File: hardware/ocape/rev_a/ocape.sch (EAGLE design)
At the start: 8 parts, among them J1 CON_HEADER_2X05-PTH+SHROUDED_A, J2 JUMPER-PTH-2-NO, P9/P8 BBB_HEADERS, U1 CAT24C256WI-GT3

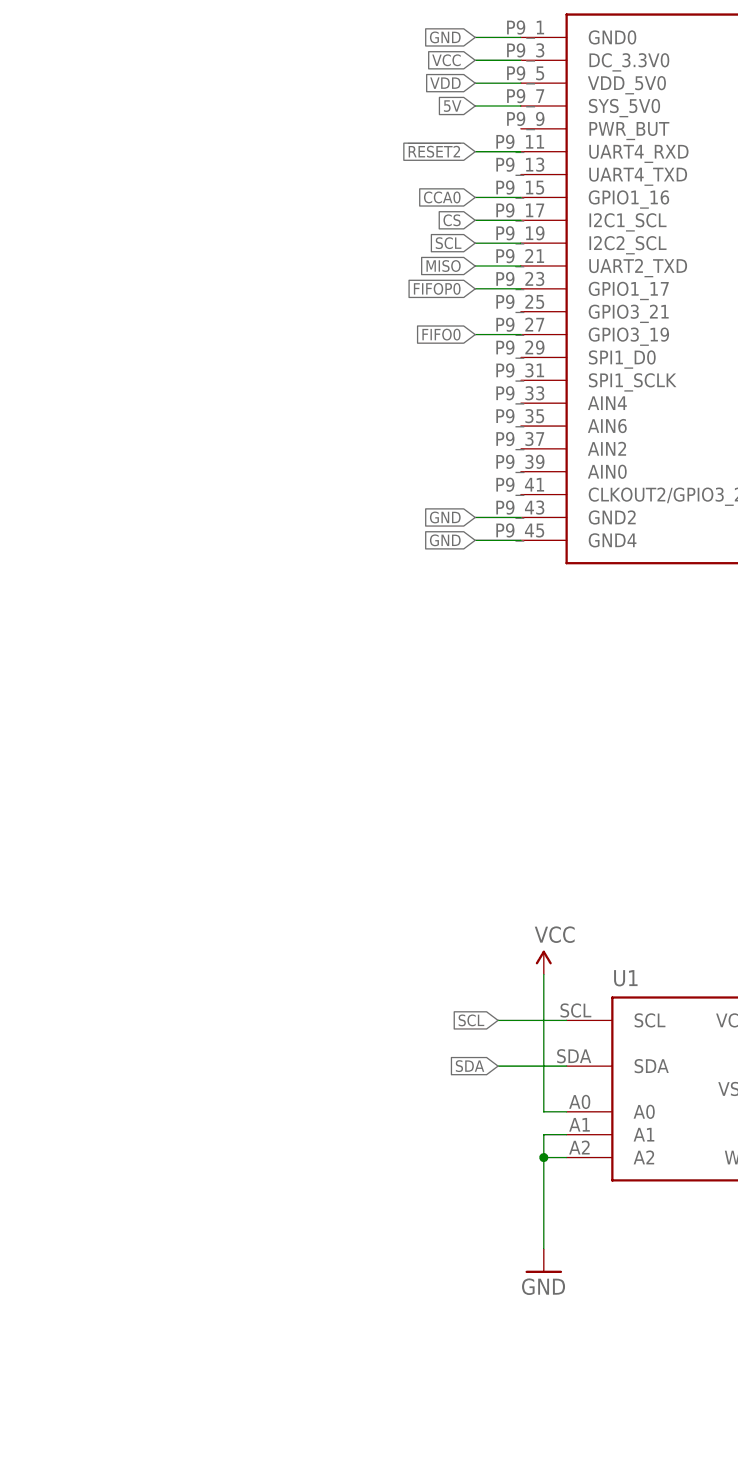
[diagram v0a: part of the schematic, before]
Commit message: new design with mountable sensor board
If the sensor board doesn't need to be attached elsewhere, it can be
attached to the BBB cape.
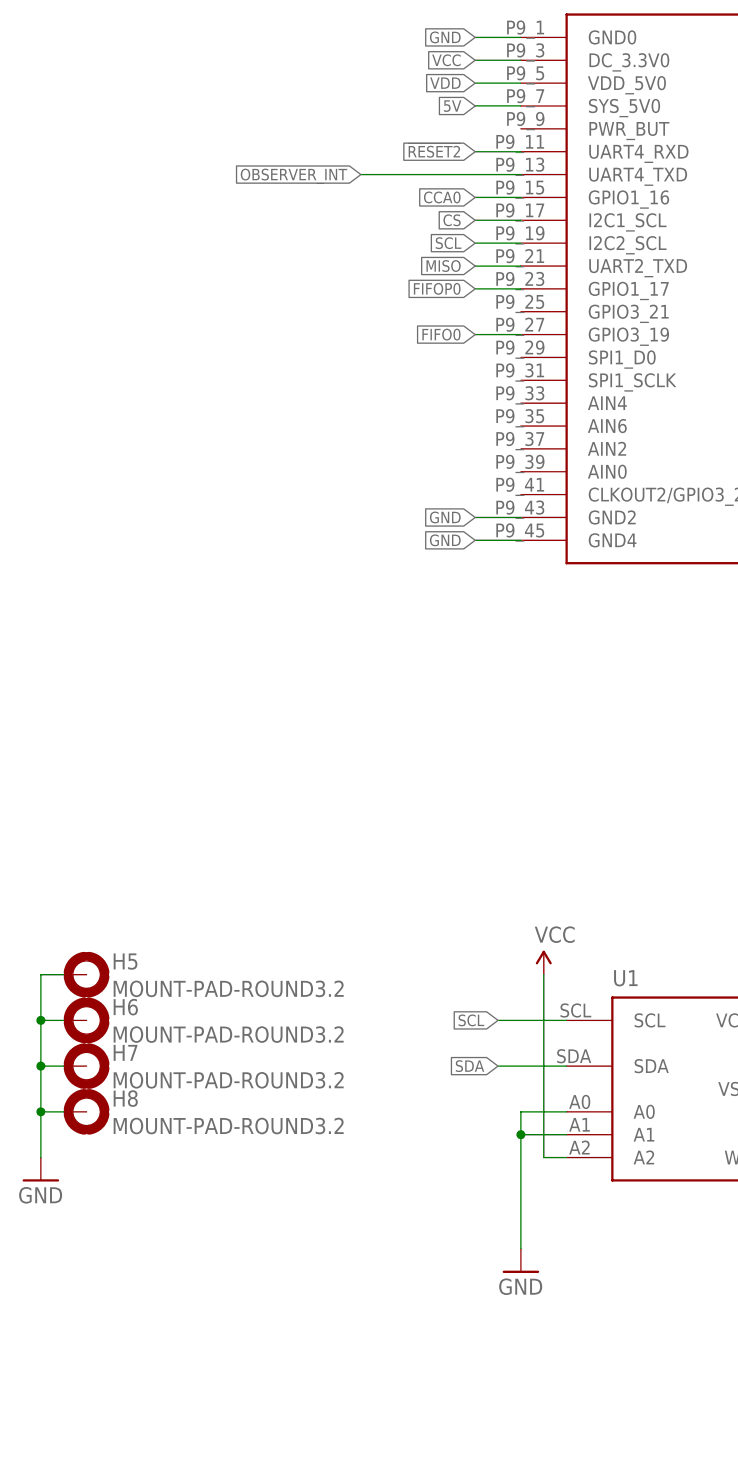
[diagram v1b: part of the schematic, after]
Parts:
- added H5, H6, H7, H8: MOUNT-PAD-ROUND3.2, holes:MOUNT-PAD-ROUND3.2
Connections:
- net GND: now also H5.MOUNT, H6.MOUNT, H7.MOUNT, H8.MOUNT, U1.A0; no longer U1.A2
- net OBSERVER_INT: now also P9/P8.UART4_TXD
- net VCC: now also U1.A2; no longer U1.A0
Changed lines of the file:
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@@
 <part name="JP1" library="pinhead" deviceset="PINHD-1X1" device=""/>
 <part name="LOGO1" library="logos" deviceset="UMICH_SOLID" device="_SMALL"/>
+<part name="H5" library="holes" deviceset="MOUNT-PAD-ROUND" device="3.2"/>
+<part name="H6" library="holes" deviceset="MOUNT-PAD-ROUND" device="3.2"/>
+<part name="H7" library="holes" deviceset="MOUNT-PAD-ROUND" device="3.2"/>
+<part name="H8" library="holes" deviceset="MOUNT-PAD-ROUND" device="3.2"/>
+<part name="GND1" library="SparkFun-Aesthetics" deviceset="GND" device=""/>
 </parts>
 <sheets>
@@
 <instance part="U1" gate="G$1" x="66.04" y="30.48"/>
 <instance part="SUPPLY1" gate="G$1" x="58.42" y="53.34"/>
-<instance part="GND7" gate="1" x="58.42" y="20.32"/>
+<instance part="GND7" gate="1" x="55.88" y="20.32"/>
 <instance part="GND8" gate="1" x="116.84" y="33.02"/>
 <instance part="C1" gate="G$1" x="116.84" y="45.72">
@@
 <instance part="JP1" gate="G$1" x="182.88" y="45.72" rot="R180"/>
 <instance part="LOGO1" gate="G$1" x="223.52" y="81.28"/>
+<instance part="H5" gate="G$1" x="7.62" y="53.34"/>
+<instance part="H6" gate="G$1" x="7.62" y="48.26"/>
+<instance part="H7" gate="G$1" x="7.62" y="43.18"/>
+<instance part="H8" gate="G$1" x="7.62" y="38.1"/>
+<instance part="GND1" gate="1" x="2.54" y="30.48"/>
 </instances>
 <busses>
@@
 </segment>
 <segment>
+<pinref part="U1" gate="G$1" pin="A0"/>
+<wire x1="60.96" y1="38.1" x2="55.88" y2="38.1" width="0.1524" layer="91"/>
+<wire x1="55.88" y1="38.1" x2="55.88" y2="35.56" width="0.1524" layer="91"/>
+<pinref part="GND7" gate="1" pin="GND"/>
+<wire x1="55.88" y1="35.56" x2="55.88" y2="22.86" width="0.1524" layer="91"/>
 <pinref part="U1" gate="G$1" pin="A1"/>
-<wire x1="60.96" y1="35.56" x2="58.42" y2="35.56" width="0.2032" layer="91"/>
-<pinref part="U1" gate="G$1" pin="A2"/>
-<wire x1="60.96" y1="33.02" x2="58.42" y2="33.02" width="0.2032" layer="91"/>
-<wire x1="58.42" y1="35.56" x2="58.42" y2="33.02" width="0.1524" layer="91"/>
-<junction x="58.42" y="33.02"/>
-<pinref part="GND7" gate="1" pin="GND"/>
-<wire x1="58.42" y1="33.02" x2="58.42" y2="22.86" width="0.1524" layer="91"/>
+<wire x1="60.96" y1="35.56" x2="55.88" y2="35.56" width="0.1524" layer="91"/>
+<junction x="55.88" y="35.56"/>
+</segment>
+<segment>
+<pinref part="H8" gate="G$1" pin="MOUNT"/>
+<wire x1="5.08" y1="38.1" x2="2.54" y2="38.1" width="0.1524" layer="91"/>
+<wire x1="2.54" y1="38.1" x2="2.54" y2="43.18" width="0.1524" layer="91"/>
+<pinref part="H7" gate="G$1" pin="MOUNT"/>
+<wire x1="2.54" y1="43.18" x2="5.08" y2="43.18" width="0.1524" layer="91"/>
+<pinref part="H6" gate="G$1" pin="MOUNT"/>
+<wire x1="5.08" y1="48.26" x2="2.54" y2="48.26" width="0.1524" layer="91"/>
+<wire x1="2.54" y1="48.26" x2="2.54" y2="43.18" width="0.1524" layer="91"/>
+<junction x="2.54" y="43.18"/>
+<pinref part="H5" gate="G$1" pin="MOUNT"/>
+<wire x1="5.08" y1="53.34" x2="2.54" y2="53.34" width="0.1524" layer="91"/>
+<wire x1="2.54" y1="53.34" x2="2.54" y2="48.26" width="0.1524" layer="91"/>
+<junction x="2.54" y="48.26"/>
+<wire x1="2.54" y1="38.1" x2="2.54" y2="33.02" width="0.1524" layer="91"/>
+<junction x="2.54" y="38.1"/>
+<pinref part="GND1" gate="1" pin="GND"/>
 </segment>
 </net>
@@
 <segment>
 <pinref part="SUPPLY1" gate="G$1" pin="VCC"/>
-<pinref part="U1" gate="G$1" pin="A0"/>
-<wire x1="58.42" y1="38.1" x2="60.96" y2="38.1" width="0.2032" layer="91"/>
-<wire x1="58.42" y1="53.34" x2="58.42" y2="38.1" width="0.1524" layer="91"/>
+<wire x1="58.42" y1="53.34" x2="58.42" y2="33.02" width="0.1524" layer="91"/>
+<pinref part="U1" gate="G$1" pin="A2"/>
+<wire x1="58.42" y1="33.02" x2="60.96" y2="33.02" width="0.1524" layer="91"/>
 </segment>
 <segment>
@@
 <label x="193.04" y="58.42" size="1.27" layer="95" xref="yes"/>
 </segment>
-</net>
+<segment>
+<pinref part="P9/P8" gate="G$1" pin="UART4_TXD"/>
+<wire x1="55.88" y1="142.24" x2="38.1" y2="142.24" width="0.1524" layer="91"/>
+<label x="38.1" y="142.24" size="1.27" layer="95" rot="R180" xref="yes"/>
+</segment>
+</net>

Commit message: basically done with observer
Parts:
- renumbered JP1 to J3
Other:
- moved on the sheet: C1, H5, H6, H7, H8, J2, R1, U1
